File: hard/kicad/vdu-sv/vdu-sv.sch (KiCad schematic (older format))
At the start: 29 parts, among them J1 IOx, J2 (S)VGA, J3 256 COLOUR, U1 74HC138, U10 74HC245, U11 74HC245, U12 74HC245, U13 74HC574, U14 74HC157, U15 74HC86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

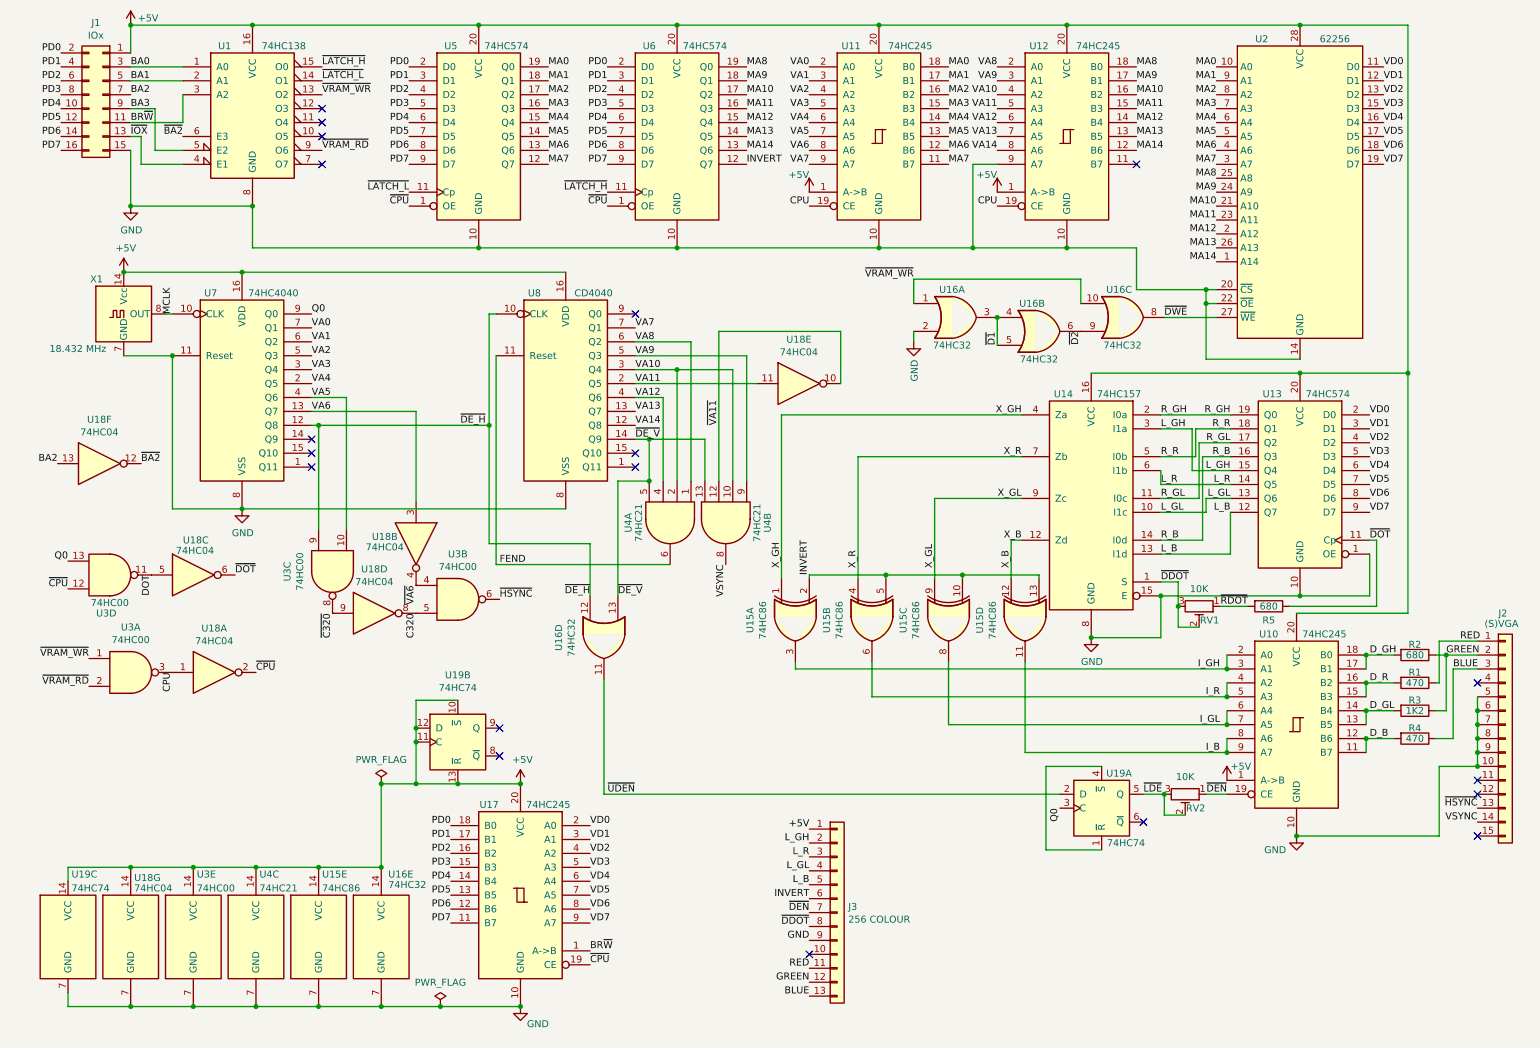
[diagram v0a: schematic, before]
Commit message: integrate 8-bit mode in VDU-SV
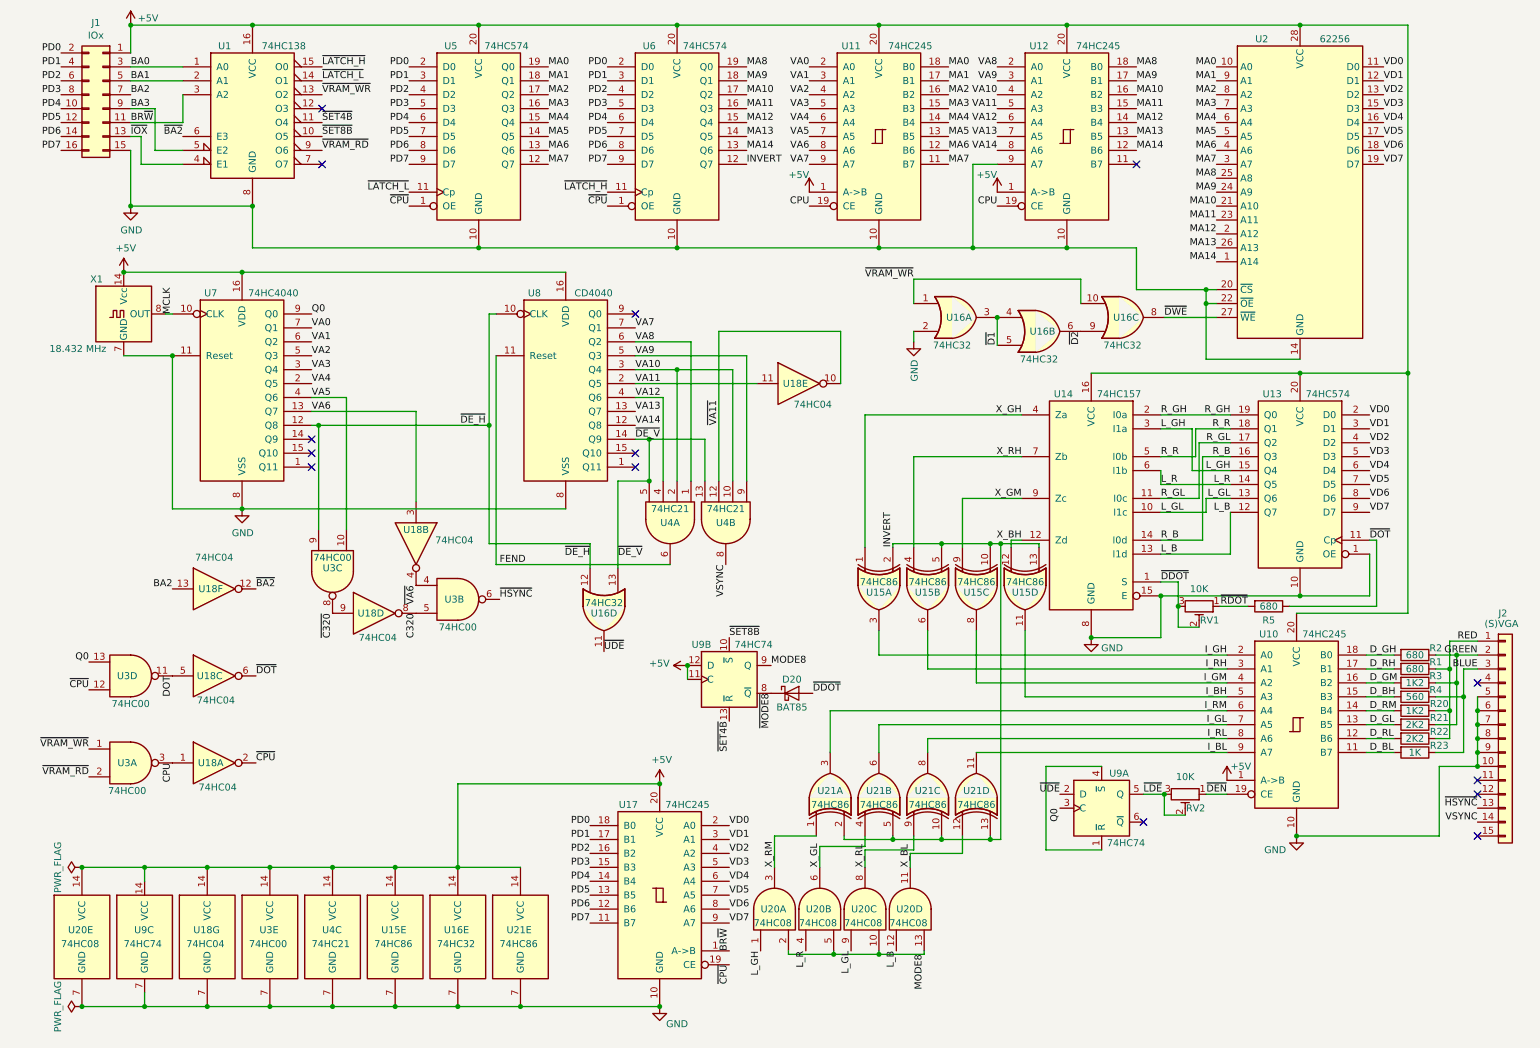
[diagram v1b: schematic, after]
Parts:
- removed J3: 256 COLOUR, Connector_PinHeader_2.54mm:PinHeader_1x13_P2.54mm_Vertical, symbol Connector_Generic:Conn_01x13
- added D20: BAT85, Diode_THT:D_DO-35_SOD27_P7.62mm_Horizontal, symbol Diode:BAT85
- added R20: 1K2, Resistor_THT:R_Axial_DIN0207_L6.3mm_D2.5mm_P2.54mm_Vertical, symbol Device:R
- added R21, R22: 2K2, Resistor_THT:R_Axial_DIN0207_L6.3mm_D2.5mm_P2.54mm_Vertical, symbol Device:R
- added R23: 1K, Resistor_THT:R_Axial_DIN0207_L6.3mm_D2.5mm_P2.54mm_Vertical, symbol Device:R
- added U20: 74HC08, Package_DIP:DIP-14_W7.62mm_Socket, symbol 74xx:74LS08
- added U21: 74HC86, Package_DIP:DIP-14_W7.62mm_Socket, symbol 74xx:74HC86
- R1: value 470 -> 680
- R4: value 470 -> 560
- renumbered U19 to U9
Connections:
- net +5V: now also U20.14 (VCC), U21.14 (VCC); no longer U9.10 (~S), U9.13 (~R)
- net BLUE: now also R23.1
- net D_GH: no longer U10.17 (B1)
- net D_GL: now also R21.2; no longer R3.2, U10.14 (B4)
- net GND: now also U20.7 (GND), U21.7 (GND)
- net GREEN: now also R21.1
- net INVERT: now also U21.10, U21.13, U21.2, U21.5
- net I_GH: no longer U10.3 (A1)
- net I_GL: now also U21.6; no longer U10.6 (A4), U15.8
- net L_B: now also U20.12
- net L_GH: now also U20.1
- net L_GL: now also U20.9
- net L_R: now also U20.4
- net RED: now also R20.1, R22.1
- net X_GL: now also U20.6, U21.4; no longer U14.9 (Zc), U15.9
- net ~DDOT: now also D20.2 (A)
- net ~SET8B: now reaches U1.10 (O5)
- net ~SET8B: now also U9.10 (~S)
- net ~SET4B: now reaches U1.11 (O4)
- net ~SET4B: now also U9.13 (~R)
- net ~MODE8: now reaches U9.8 (~Q)
- net ~MODE8: now also D20.1 (K)
- net MODE8: now reaches U9.9 (Q)
- net MODE8: now also U20.10, U20.13, U20.2, U20.5
- removed net D_B: R4.2, U10.11 (B7), U10.12 (B6)
- removed net D_R: R1.2, U10.15 (B3), U10.16 (B2)
- removed net I_B: U10.8 (A6), U10.9 (A7), U15.11
- removed net I_R: U10.4 (A2), U10.5 (A3), U15.6
- net X_B renamed X_BH
- net X_R renamed X_RH
- net ~UDEN renamed ~UDE
- new net D_BH: R4.2, U10.15 (B3)
- new net D_BL: R23.2, U10.11 (B7)
- new net D_GM: R3.2, U10.16 (B2)
- new net D_RH: R1.2, U10.17 (B1)
- new net D_RL: R22.2, U10.12 (B6)
- new net D_RM: R20.2, U10.14 (B4)
- new net I_BH: U10.5 (A3), U15.11
- new net I_BL: U10.9 (A7), U21.11
- new net I_GM: U10.4 (A2), U15.8
- new net I_RH: U10.3 (A1), U15.6
- new net I_RL: U10.8 (A6), U21.8
- new net I_RM: U10.6 (A4), U21.3
- new net X_BL: U20.11, U21.12
- new net X_GM: U14.9 (Zc), U15.9
- new net X_RL: U20.8, U21.9
- new net X_RM: U20.3, U21.1
- no-connect marks 19 -> 14
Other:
- moved on the sheet: R1, R3, R4, U15A, U15B, U15C, U15D, U15E, U16D, U16E, U17, U18A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

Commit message: add IDC and shuffle RAM pins
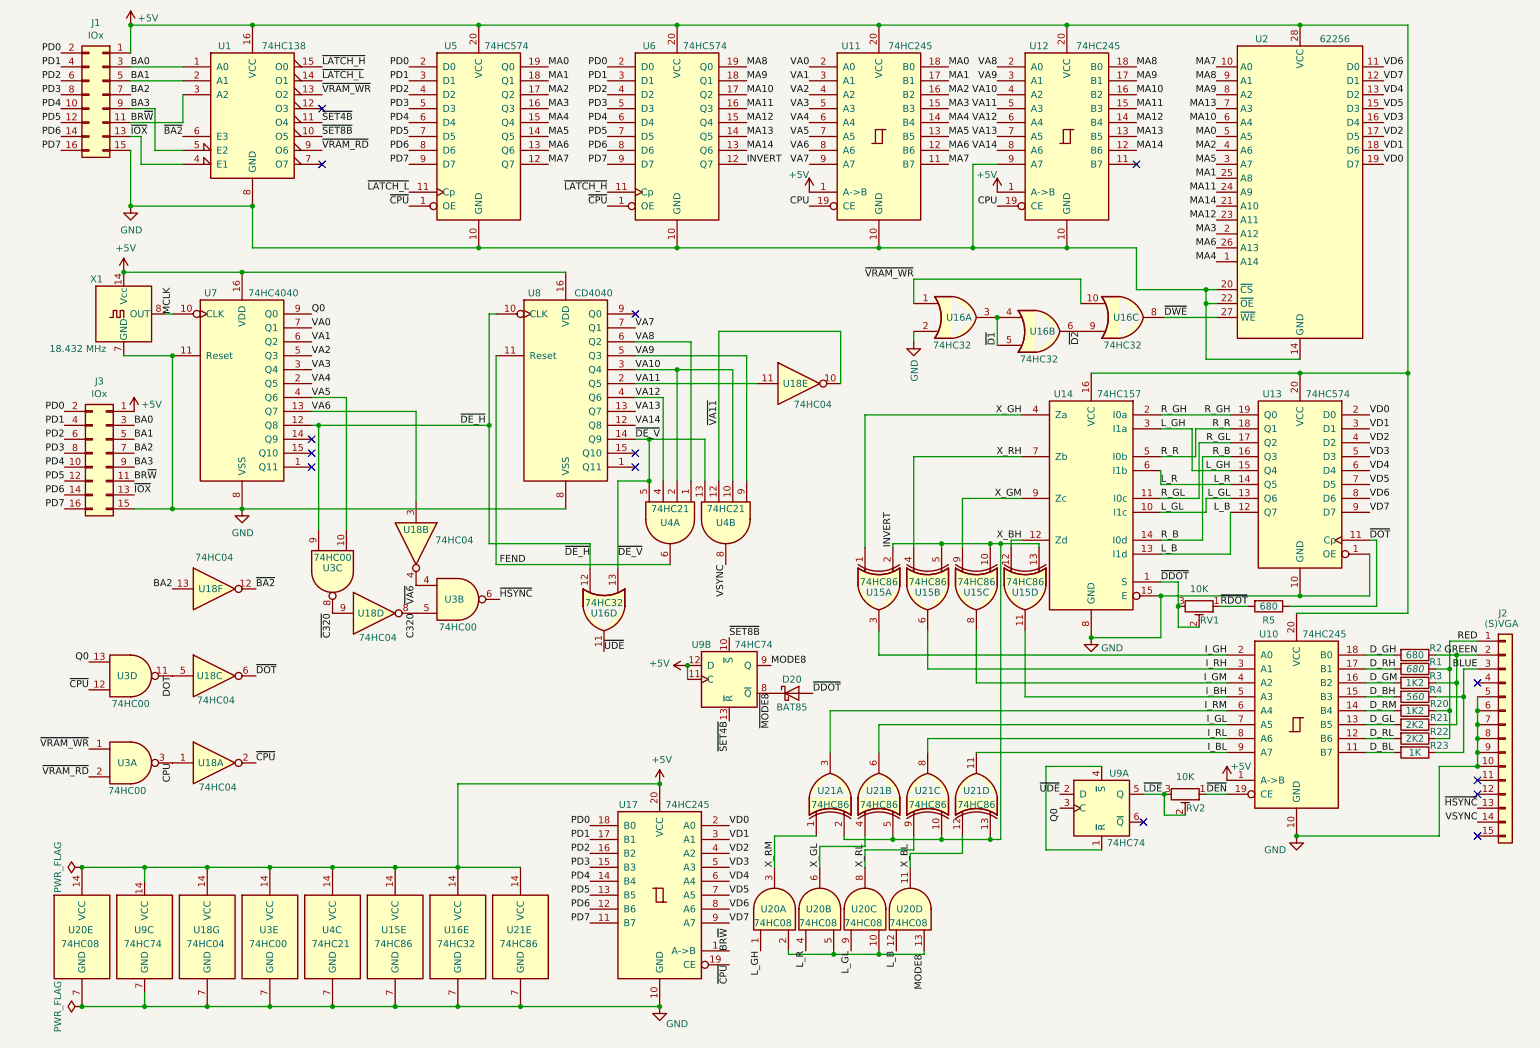
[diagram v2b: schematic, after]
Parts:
- added J3: IOx, Connector_IDC:IDC-Header_2x08_P2.54mm_Vertical, symbol Connector_Generic:Conn_02x08_Odd_Even
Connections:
- net +5V: now also J3.1 (Pin_1)
- net BA0: now also J3.3 (Pin_3)
- net BA1: now also J3.5 (Pin_5)
- net BA2: now also J3.7 (Pin_7)
- net BA3: now also J3.9 (Pin_9)
- net BR~W: now also J3.11 (Pin_11)
- net GND: now also J3.15 (Pin_15)
- net MA0: now also U2.5 (A5); no longer U2.10 (A0)
- net MA1: now also U2.25 (A8); no longer U2.9 (A1)
- net MA10: now also U2.6 (A4); no longer U2.21 (A10)
- net MA11: now also U2.24 (A9); no longer U2.23 (A11)
- net MA12: now also U2.23 (A11); no longer U2.2 (A12)
- net MA13: now also U2.7 (A3); no longer U2.26 (A13)
- net MA14: now also U2.21 (A10); no longer U2.1 (A14)
- net MA2: now also U2.4 (A6); no longer U2.8 (A2)
- net MA3: now also U2.2 (A12); no longer U2.7 (A3)
- net MA4: now also U2.1 (A14); no longer U2.6 (A4)
- net MA5: now also U2.3 (A7); no longer U2.5 (A5)
- net MA6: now also U2.26 (A13); no longer U2.4 (A6)
- net MA7: now also U2.10 (A0); no longer U2.3 (A7)
- net MA8: now also U2.9 (A1); no longer U2.25 (A8)
- net MA9: now also U2.8 (A2); no longer U2.24 (A9)
- net PD0: now also J3.2 (Pin_2)
- net PD1: now also J3.4 (Pin_4)
- net PD2: now also J3.6 (Pin_6)
- net PD3: now also J3.8 (Pin_8)
- net PD4: now also J3.10 (Pin_10)
- net PD5: now also J3.12 (Pin_12)
- net PD6: now also J3.14 (Pin_14)
- net PD7: now also J3.16 (Pin_16)
- net VD0: now also U2.19 (D7); no longer U2.11 (D0)
- net VD1: now also U2.18 (D6); no longer U2.12 (D1)
- net VD2: now also U2.17 (D5); no longer U2.13 (D2)
- net VD3: now also U2.16 (D4); no longer U2.15 (D3)
- net VD4: now also U2.13 (D2); no longer U2.16 (D4)
- net VD5: now also U2.15 (D3); no longer U2.17 (D5)
- net VD6: now also U2.11 (D0); no longer U2.18 (D6)
- net VD7: now also U2.12 (D1); no longer U2.19 (D7)
- net ~IOX: now also J3.13 (Pin_13)
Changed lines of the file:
@@
 P 10450 5200
 F 0 "R1" V 10400 5350 50  0000 C CNN
-F 1 "680" V 10450 5200 50  0000 C CNN
+F 1 "680" V 10450 5200 50  0000 C CIN
 F 2 "Resistor_THT:R_Axial_DIN0207_L6.3mm_D2.5mm_P2.54mm_Vertical" V 10380 5200 50  0001 C CNN
 F 3 "~" H 10450 5200 50  0001 C CNN
@@
 P 10450 5400
 F 0 "R4" V 10400 5550 50  0000 C CNN
-F 1 "560" V 10450 5400 50  0000 C CNN
+F 1 "560" V 10450 5400 50  0000 C CIN
 F 2 "Resistor_THT:R_Axial_DIN0207_L6.3mm_D2.5mm_P2.54mm_Vertical" V 10380 5400 50  0001 C CNN
 F 3 "~" H 10450 5400 50  0001 C CNN
@@
 Text Label 8450 1475 0    50   ~ 0
 MA14
+Text Label 9025 975  2    50   ~ 0
+MA8
+Text Label 9025 1075 2    50   ~ 0
+MA9
+Text Label 9025 1275 2    50   ~ 0
+MA10
+Text Label 9025 1775 2    50   ~ 0
+MA11
+Text Label 9025 1975 2    50   ~ 0
+MA12
+Text Label 9025 1175 2    50   ~ 0
+MA13
+Text Label 9025 1875 2    50   ~ 0
+MA14
+Text Label 9025 1375 2    50   ~ 0
+MA0
 Text Label 9025 1675 2    50   ~ 0
-MA8
-Text Label 9025 1775 2    50   ~ 0
-MA9
-Text Label 9025 1875 2    50   ~ 0
-MA10
-Text Label 9025 1975 2    50   ~ 0
-MA11
+MA1
+Text Label 9025 1475 2    50   ~ 0
+MA2
 Text Label 9025 2075 2    50   ~ 0
-MA12
+MA3
+Text Label 9025 2275 2    50   ~ 0
+MA4
+Text Label 9025 1575 2    50   ~ 0
+MA5
 Text Label 9025 2175 2    50   ~ 0
-MA13
-Text Label 9025 2275 2    50   ~ 0
-MA14
+MA6
 Text Label 9025 875  2    50   ~ 0
-MA0
-Text Label 9025 975  2    50   ~ 0
-MA1
-Text Label 9025 1075 2    50   ~ 0
-MA2
-Text Label 9025 1175 2    50   ~ 0
-MA3
-Text Label 9025 1275 2    50   ~ 0
-MA4
-Text Label 9025 1375 2    50   ~ 0
-MA5
-Text Label 9025 1475 2    50   ~ 0
-MA6
-Text Label 9025 1575 2    50   ~ 0
 MA7
+Text Label 10225 1575 0    50   ~ 0
+VD0
+Text Label 10225 1475 0    50   ~ 0
+VD1
+Text Label 10225 1375 0    50   ~ 0
+VD2
+Text Label 10225 1275 0    50   ~ 0
+VD3
+Text Label 10225 1075 0    50   ~ 0
+VD4
+Text Label 10225 1175 0    50   ~ 0
+VD5
 Text Label 10225 875  0    50   ~ 0
-VD0
+VD6
 Text Label 10225 975  0    50   ~ 0
-VD1
-Text Label 10225 1075 0    50   ~ 0
-VD2
-Text Label 10225 1175 0    50   ~ 0
-VD3
-Text Label 10225 1275 0    50   ~ 0
-VD4
-Text Label 10225 1375 0    50   ~ 0
-VD5
-Text Label 10225 1475 0    50   ~ 0
-VD6
-Text Label 10225 1575 0    50   ~ 0
 VD7
 $Comp
@@
 Wire Wire Line
 	10800 5200 10900 5200
+$Comp
+L Connector_Generic:Conn_02x08_Odd_Even J3
+U 1 1 65AB675D
+P 1050 3650
+F 0 "J3" H 1100 4167 50  0000 C CNN
+F 1 "IOx" H 1100 4076 50  0000 C CNN
+F 2 "Connector_IDC:IDC-Header_2x08_P2.54mm_Vertical" H 1050 3650 50  0001 C CNN
+F 3 "~" H 1050 3650 50  0001 C CNN
+	1    1050 3650
+	-1   0    0    -1
+$EndComp
+$Comp
+L power:+5V #PWR0114
+U 1 1 65AB6767
+P 1250 3350
+F 0 "#PWR0114" H 1250 3200 50  0001 C CNN
+F 1 "+5V" H 1375 3400 50  0000 C CNN
+F 2 "" H 1250 3350 50  0001 C CNN
+F 3 "" H 1250 3350 50  0001 C CNN
+	1    1250 3350
+	1    0    0    -1
+$EndComp
+Text Label 750  3350 2    50   ~ 0
+PD0
+Text Label 750  3450 2    50   ~ 0
+PD1
+Text Label 750  3550 2    50   ~ 0
+PD2
+Text Label 750  3650 2    50   ~ 0
+PD3
+Text Label 750  3750 2    50   ~ 0
+PD4
+Text Label 750  3850 2    50   ~ 0
+PD5
+Text Label 750  3950 2    50   ~ 0
+PD6
+Text Label 750  4050 2    50   ~ 0
+PD7
+Text Label 1250 3450 0    50   ~ 0
+BA0
+Text Label 1250 3550 0    50   ~ 0
+BA1
+Text Label 1250 3650 0    50   ~ 0
+BA2
+Text Label 1250 3750 0    50   ~ 0
+BA3
+Text Label 1250 3850 0    50   ~ 0
+BR~W
+Text Label 1250 3950 0    50   ~ 0
+~IOX
+Wire Wire Line
+	1250 4050 1525 4050
+Connection ~ 1525 4050
 $EndSCHEMATC
